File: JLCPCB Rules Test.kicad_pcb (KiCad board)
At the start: 4 copper layers, 157 x 123 mm, 33 parts, among them J101 Conn_01x04, J102 Conn_01x04

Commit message: update rules
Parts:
- moved REF** 3.87 mm to (65.1, 112.3)
- moved REF** 3.87 mm to (34.3, 112.2)
- moved REF** 3.87 mm to (53.0, 92.9)
- moved REF** 3.87 mm to (49.3, 112.2)
- moved REF** 3.87 mm to (35.3, 127.9)
- moved REF** 3.87 mm to (36.0, 92.9)
- moved REF** 3.87 mm to (43.3, 127.9)
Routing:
- net Net-(J101-Pin_4): track 160.3 -> 166.0 mm
- net Net-(J101-Pin_3): track 85.6 -> 86.8 mm, vias 11 -> 13
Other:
- board text added: "0.14mm/0.25mm Via FAIL"
- board text added: "0.15mm/(0.25/0.3mm) Via PASS (special)"
- board text added: "0.15mm/0.24mm Via FAIL"
- board text added: "0.1mm FAIL 0.30mm FAIL 0.40mm PASS"
- board text added: "0.25mm/(0.35/0.4mm) Via PASS (special)"
- board text added: "0.2mm/(0.3/0.35mm) Via PASS (special)"
- board text added: "0.3mm/(0.4/0.45mm) Via PASS (standard)"
- board text added: "Min. Via hole size AND Min. Via diameter"
- board text added: "Not tested: Any tolerances Min. Castellated Holes Drill Hole Size Min 0.2mm (Redundant. NPTH min is 0.5mm. Via min is 0.2mm already) Rectangle Hole/Slot"
- board text removed: "(Going to 0.4mm adds cost)"
- board text removed: "0.18mm FAIL 0.20mm PASS"
- board text removed: "0.19mm/0.8mm Via FAIL"
- board text removed: "0.2mm/0.44mm Via FAIL"
- board text removed: "0.2mm/0.45mm Via PASS"
- board text removed: "0.2mm/0.8mm Via PASS"
- board text removed: "Min. Via diameter"
- board text removed: "Min. Via hole size"
- board text removed: "Not tested: Any tolerances Min. Castellated Holes Drill Hole Size Min 0.2mm (Redundant. NPTH min is 0.5mm. Via min is 0.2mm already) Rectangle Hole/Slot Minimum Annular Ring (0.2/0.45mm vias are clearly allowed which is an annular ring of 0.125mm and PTH of 0.2mm. This contradicts that by saying min. is 0.13mm annular ring and 0.3mm PTH.)"

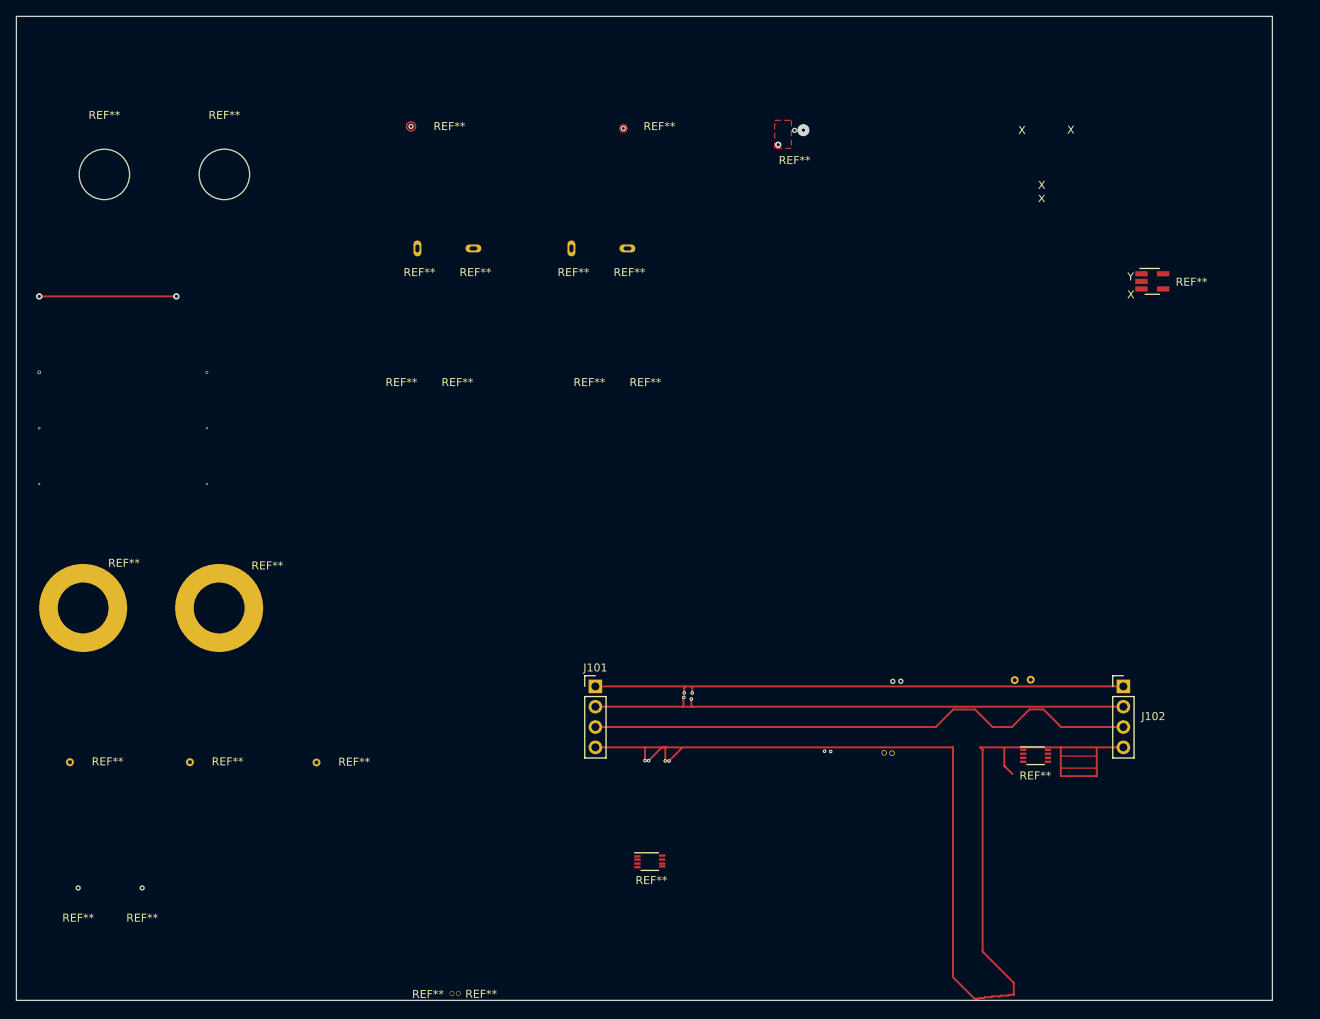
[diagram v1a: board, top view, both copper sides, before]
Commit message: Misc. improvements. More support for diff. layer counts and 2oz Cu.
- Added 2-layer via size test to PCB
- Edited min. via size and diameter test cases to only include primary limitations, not extreme limitations. Example: On 0.3mm/(0.4/0.45mm), the rule only tests for 0.3/0.45mm, so the PCB text was edited to reflect this and match the test via sizes shown. Also, some of the vias for the special 4-layer sizes had the extreme size for the test via so they would always fail the DRC check. These vias were adjusted to match the rules.
- Fixed via sizes used for min clearance testing to use 0.3/0.5mm via size so they wouldn't trigger via size errors even with 2-layer clearance rules selected
- Redid track to track test, added tests for all spacing options
- Cleaned up trace to outline tests
- Added milled slot edge clearance example test
- Removed specific edge cuts to track rule since edge_clearance already covers that too.
- Reduced line thickness for board outline on edgecuts layer to make Trace to Outline test clearer
- Removed extra footprint that was unused
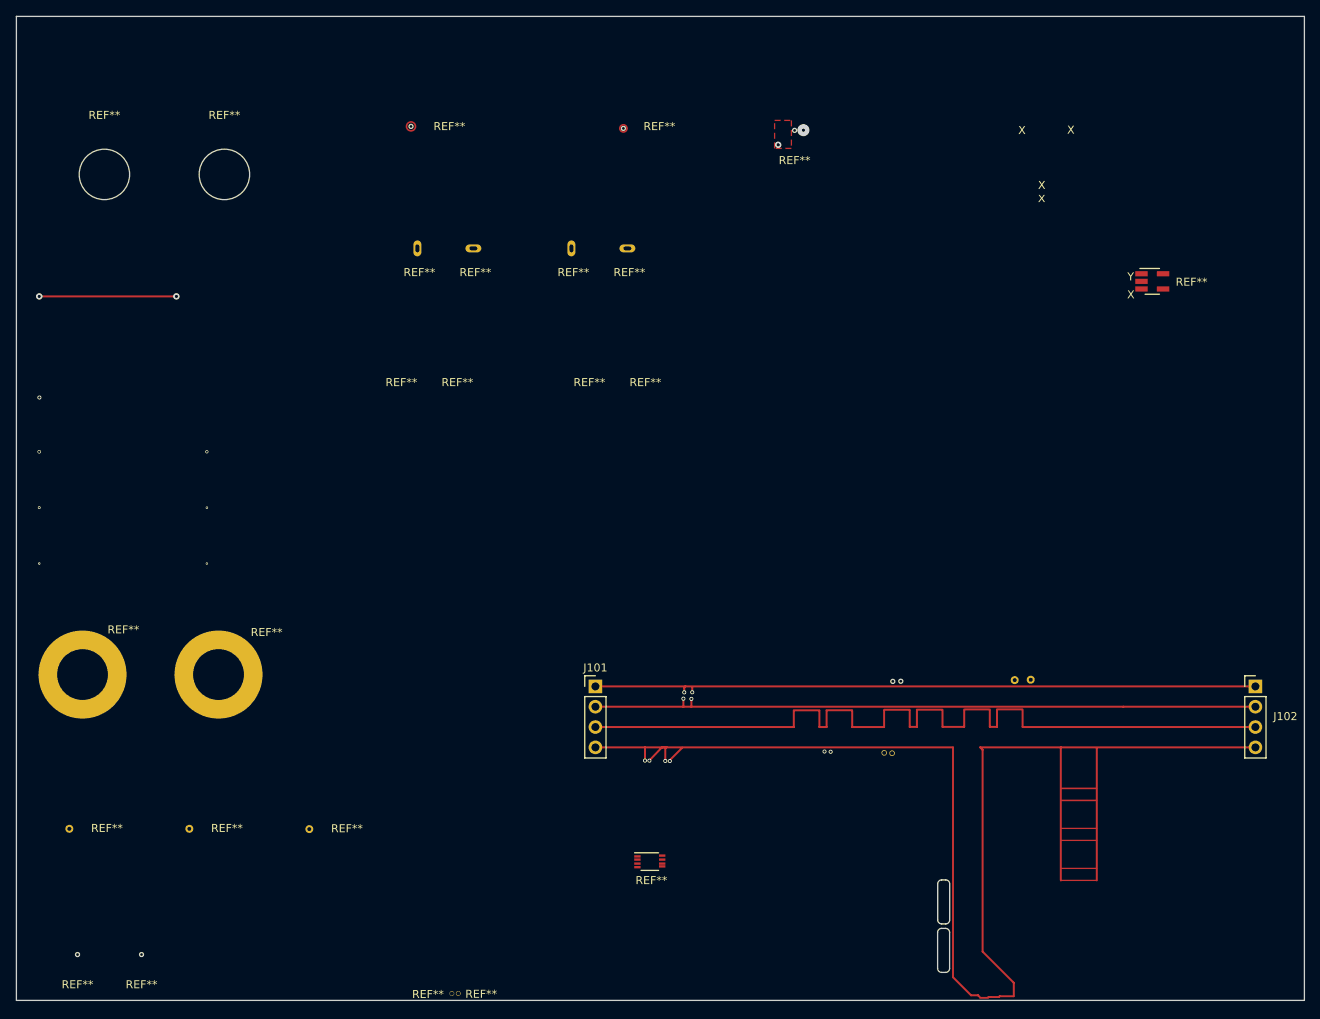
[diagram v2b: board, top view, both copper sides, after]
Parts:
- removed the REF** at (155.0, 111.4)
- moved J102 16.5 mm to (182.5, 102.8)
- moved REF** 8.37 mm to (64.2, 120.6)
- moved REF** 8.33 mm to (35.3, 136.3)
- moved REF** 8.33 mm to (43.3, 136.3)
- moved REF** 8.33 mm to (34.2, 120.5)
- moved REF** 8.33 mm to (52.9, 101.3)
- moved REF** 8.33 mm to (49.2, 120.5)
- moved REF** 8.33 mm to (35.9, 101.3)
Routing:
- net Net-(J101-Pin_4): track 166.0 -> 217.9 mm
- net Net-(J101-Pin_3): track 86.8 -> 124.0 mm, vias 13 -> 14
- net Net-(J101-Pin_2): track 68.1 -> 84.6 mm
- net Net-(J101-Pin_1): track 67.3 -> 83.7 mm
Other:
- board size 157 x 123 mm -> 161 x 123 mm
- board text added: "(Assuming by {dblquote}Pad{dblquote} they mean PTH hole) < 0.5mm FAIL (Actually impossible with 0.25mm annular ring requirement for PTH + 0.127mm pad to pad clearance) (Ignore annular width violation)"
- board text added: "0.08mm FAIL"
- board text added: "0.09mm PASS"
- board text added: "0.12mm FAIL"
- board text added: "0.13mm PASS"
- board text added: "0.14mm/0.3mm Via FAIL"
- board text added: "0.15mm/0.29mm Via FAIL"
- board text added: "0.15mm/0.3mm Via PASS (4-layer special)"
- board text added: "0.19mm FAIL"
- board text added: "0.20mm FAIL 0.30mm PASS (Routed) 0.40mm PASS (V-score)"
- board text added: "0.245mm FAIL 0.27mm PASS"
- board text added: "0.25mm FAIL 0.26mm PASS"
- board text added: "0.25mm/0.4mm Via PASS (4-layer special)"
- board text added: "0.2mm PASS"
- board text added: "0.2mm PASS (2 oz copper) 0.19mm FAIL 0.127mm PASS (2-layer) 0.12mm FAIL 0.09mm PASS (4-layer) 0.089mm FAIL"
- board text added: "0.2mm/0.35mm Via PASS (4-layer special)"
- board text added: "0.3mm/0.45mm Via PASS (4-layer standard)"
- board text added: "0.3mm/0.5mm Via PASS (2-layer)"
- board text added: "0.49mm FAIL 0.53mm PASS"
- board text added: "0.50/0.99mm PTH FAIL"
- board text added: "2-layer"
- board text added: "2-oz Copper"
- board text added: "4-layer"
- board text added: "Trace to Outline"
- board text added: "Trace to Outline (Milled Slot Example) 0.29mm FAIL 0.3mm PASS"
- board text removed: "(PTH) < 0.5mm FAIL (Actually impossibly with 0.25mm annular ring requirement for PTH + 0.127mm pad to pad clearance) (Ignore annular width violation)"
- board text removed: "0.14mm/0.25mm Via FAIL"
- board text removed: "0.15mm/(0.25/0.3mm) Via PASS (special)"
- board text removed: "0.15mm/0.24mm Via FAIL"
- board text removed: "0.1mm FAIL 0.30mm FAIL 0.40mm PASS"
- board text removed: "0.2513mm FAIL 0.26mm PASS"
- board text removed: "0.252mm FAIL 0.29mm PASS"
- board text removed: "0.25mm/(0.35/0.4mm) Via PASS (special)"
- board text removed: "0.2mm/(0.3/0.35mm) Via PASS (special)"
- board text removed: "0.35mm FAIL 0.55mm PASS"
- board text removed: "0.3mm/(0.4/0.45mm) Via PASS (standard)"
- board text removed: "0.50/0.99 PTH FAIL"
- board text removed: "3.5mil PASS 3.4mil FAIL"
- board text removed: "3.74mil (0.095mm) PASS 3.35mil (0.085mm) FAIL"
- board text removed: "Trace to Outline (Routed)"
